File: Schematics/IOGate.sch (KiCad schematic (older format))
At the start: 11 parts, among them J1 Conn_02x03_Odd_Even, J5 Conn_01x04_Male, U3 AD8418

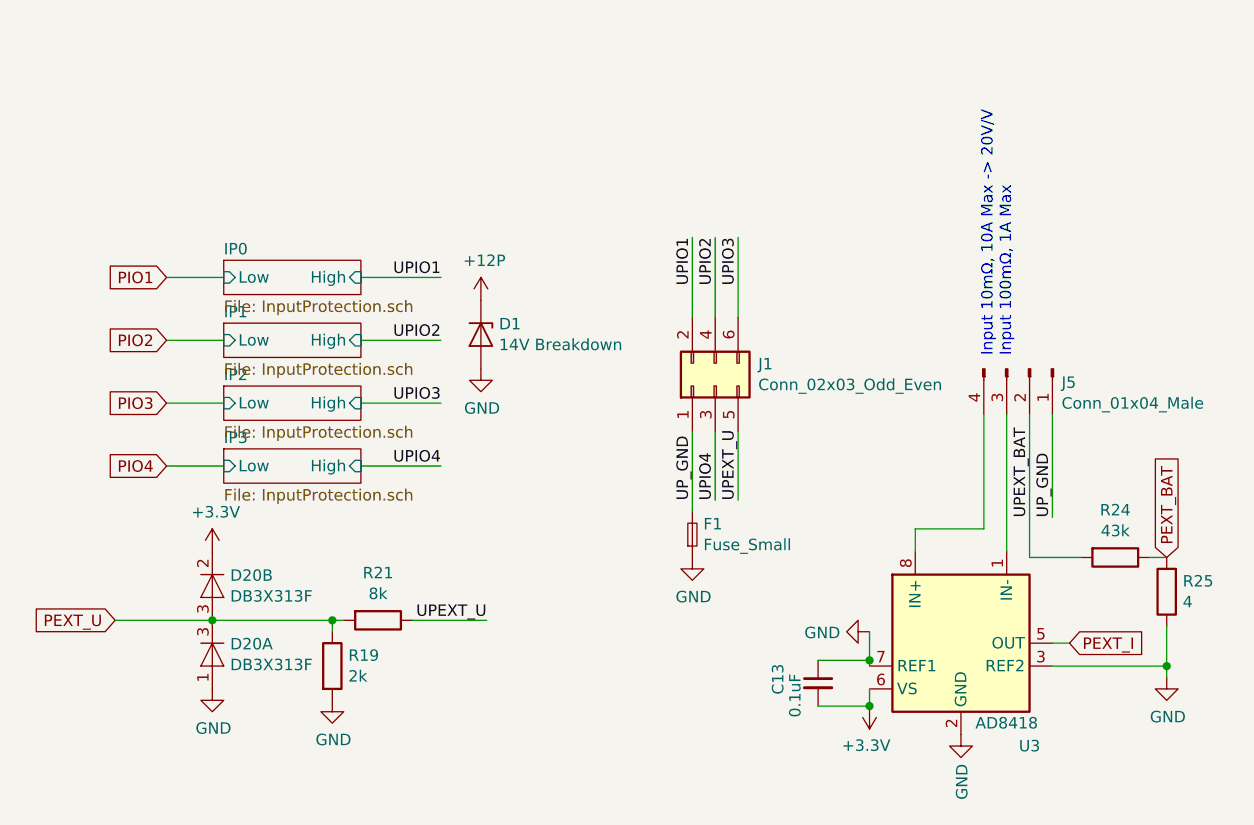
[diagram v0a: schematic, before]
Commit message: Adjusted resistor values
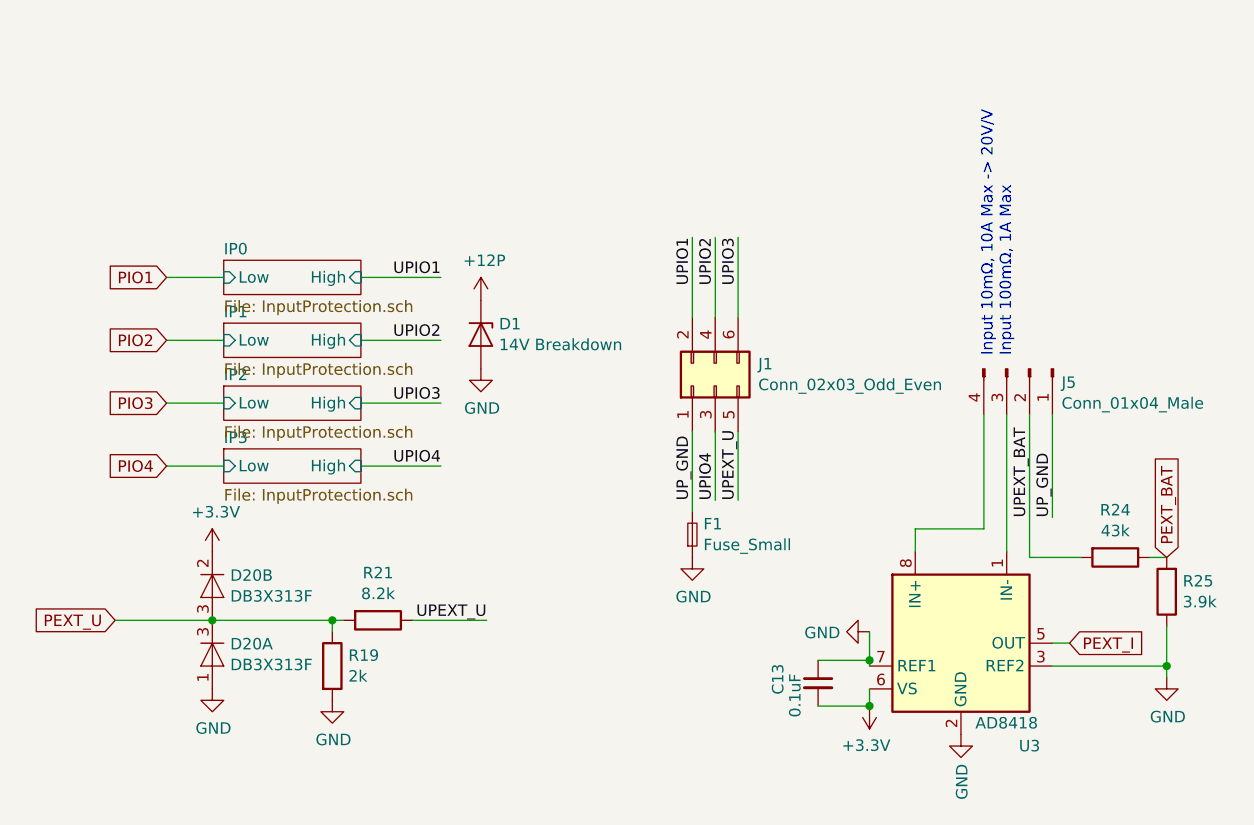
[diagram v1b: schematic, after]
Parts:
- R21: value 8k -> 8.2k
- R25: value 4 -> 3.9k
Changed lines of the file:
@@
 P 7100 4400
 F 0 "R21" V 6893 4400 50  0000 C CNN
-F 1 "8k" V 6984 4400 50  0000 C CNN
+F 1 "8.2k" V 6984 4400 50  0000 C CNN
 F 2 "Resistor_SMD:R_0805_2012Metric" V 7030 4400 50  0001 C CNN
 F 3 "~" H 7100 4400 50  0001 C CNN
@@
 P 10550 4275
 F 0 "R25" H 10480 4229 50  0000 R CNN
-F 1 "4" H 10480 4320 50  0000 R CNN
+F 1 "3.9k" H 10480 4320 50  0000 R CNN
 F 2 "Resistor_SMD:R_0805_2012Metric" V 10480 4275 50  0001 C CNN
 F 3 "~" H 10550 4275 50  0001 C CNN
